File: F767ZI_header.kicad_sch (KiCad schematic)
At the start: 24 parts, among them J1 I2C2_MD, J2 CAN1, J3 CAN2, J4 UART, J5 PowerBoard, J6 EMERSW_CON, J7 I2C1_default, J9 RESET_SW, SW1 SW_Push, U1 MCP2562-E-P, U2 MCP2562-E-P

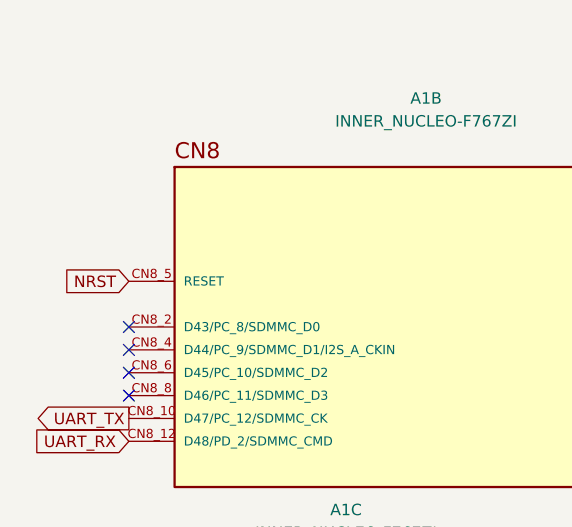
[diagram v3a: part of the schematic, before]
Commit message: SCH: Add CN8_1 to NUCLEO lib
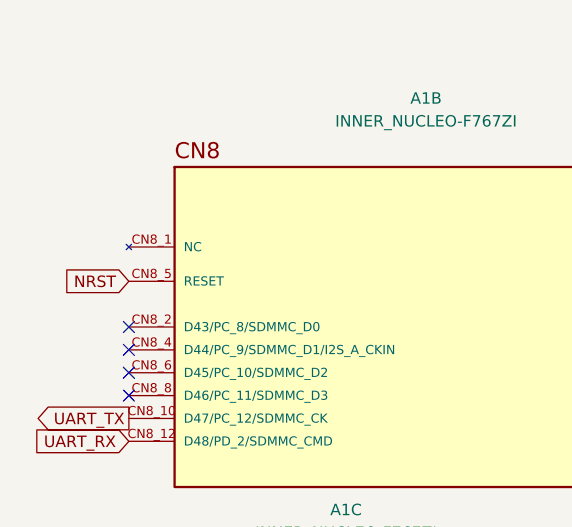
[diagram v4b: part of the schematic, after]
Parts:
- A1: footprint NUCLEO-F767ZI:INNER_ST_NUCLEO-F767ZI -> NUCLEO-F767ZI:ST_NUCLEO-F767ZI
- C1, C2, C3, C4: footprint (none) -> Capacitor_THT:C_Disc_D5.0mm_W2.5mm_P2.50mm
- J7: footprint (none) -> Connector_JST:JST_XA_B04B-XASK-1_1x04_P2.50mm_Vertical
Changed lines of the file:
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@@
 			)
 		)
-		(property "Footprint" ""
+		(property "Footprint" "Capacitor_THT:C_Disc_D5.0mm_W2.5mm_P2.50mm"
 			(at 156.21 91.44 0)
 			(effects
@@
 			)
 		)
-		(property "Footprint" ""
+		(property "Footprint" "Capacitor_THT:C_Disc_D5.0mm_W2.5mm_P2.50mm"
 			(at 156.21 130.81 0)
 			(effects
@@
 	)
 	(symbol
+		(lib_name "INNER_NUCLEO-F767ZI_1")
 		(lib_id "NUCLEO-F767ZI:INNER_NUCLEO-F767ZI")
 		(at 67.31 54.61 0)
@@
 			)
 		)
-		(property "Footprint" "NUCLEO-F767ZI:INNER_ST_NUCLEO-F767ZI"
+		(property "Footprint" "NUCLEO-F767ZI:ST_NUCLEO-F767ZI"
 			(at 67.31 54.61 0)
 			(effects
@@
 		(pin "CN10_12"
 		)
+		(pin "CN8_1-UA"
+		)
+		(pin "CN8_1-UC"
+		)
+		(pin "CN8_1"
+		)
+		(pin "CN8_1-UD"
+		)
 		(instances
 			(project "F767ZI_header"
@@
 			)
 		)
-		(property "Footprint" "NUCLEO-F767ZI:INNER_ST_NUCLEO-F767ZI"
+		(property "Footprint" "NUCLEO-F767ZI:ST_NUCLEO-F767ZI"
 			(at 232.41 50.8 0)
 			(effects
@@
 			)
 		)
-		(property "Footprint" ""
+		(property "Footprint" "Connector_JST:JST_XA_B04B-XASK-1_1x04_P2.50mm_Vertical"
 			(at 138.43 149.86 0)
 			(effects
@@
 			)
 		)
-		(property "Footprint" "NUCLEO-F767ZI:INNER_ST_NUCLEO-F767ZI"
+		(property "Footprint" "NUCLEO-F767ZI:ST_NUCLEO-F767ZI"
 			(at 57.15 109.22 0)
 			(effects
@@
 			)
 		)
-		(property "Footprint" ""
+		(property "Footprint" "Capacitor_THT:C_Disc_D5.0mm_W2.5mm_P2.50mm"
 			(at 147.32 91.44 0)
 			(effects
@@
 			)
 		)
-		(property "Footprint" "NUCLEO-F767ZI:INNER_ST_NUCLEO-F767ZI"
+		(property "Footprint" "NUCLEO-F767ZI:ST_NUCLEO-F767ZI"
 			(at 242.57 110.49 0)
 			(effects
@@
 			)
 		)
-		(property "Footprint" ""
+		(property "Footprint" "Capacitor_THT:C_Disc_D5.0mm_W2.5mm_P2.50mm"
 			(at 147.32 130.81 0)
 			(effects

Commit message: SCH&PCB: Fix NUCLEO ilb
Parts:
- A1: footprint NUCLEO-F767ZI:ST_NUCLEO-F767ZI -> NUCLEO-F767ZI:INNER_ST_NUCLEO-F767ZI
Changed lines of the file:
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@@
 			)
 		)
-		(property "Footprint" "NUCLEO-F767ZI:ST_NUCLEO-F767ZI"
+		(property "Footprint" "NUCLEO-F767ZI:INNER_ST_NUCLEO-F767ZI"
 			(at 67.31 54.61 0)
 			(effects
@@
 			)
 		)
-		(property "Footprint" "NUCLEO-F767ZI:ST_NUCLEO-F767ZI"
+		(property "Footprint" "NUCLEO-F767ZI:INNER_ST_NUCLEO-F767ZI"
 			(at 232.41 50.8 0)
 			(effects
@@
 			)
 		)
-		(property "Footprint" "NUCLEO-F767ZI:ST_NUCLEO-F767ZI"
+		(property "Footprint" "NUCLEO-F767ZI:INNER_ST_NUCLEO-F767ZI"
 			(at 57.15 109.22 0)
 			(effects
@@
 			)
 		)
-		(property "Footprint" "NUCLEO-F767ZI:ST_NUCLEO-F767ZI"
+		(property "Footprint" "NUCLEO-F767ZI:INNER_ST_NUCLEO-F767ZI"
 			(at 242.57 110.49 0)
 			(effects

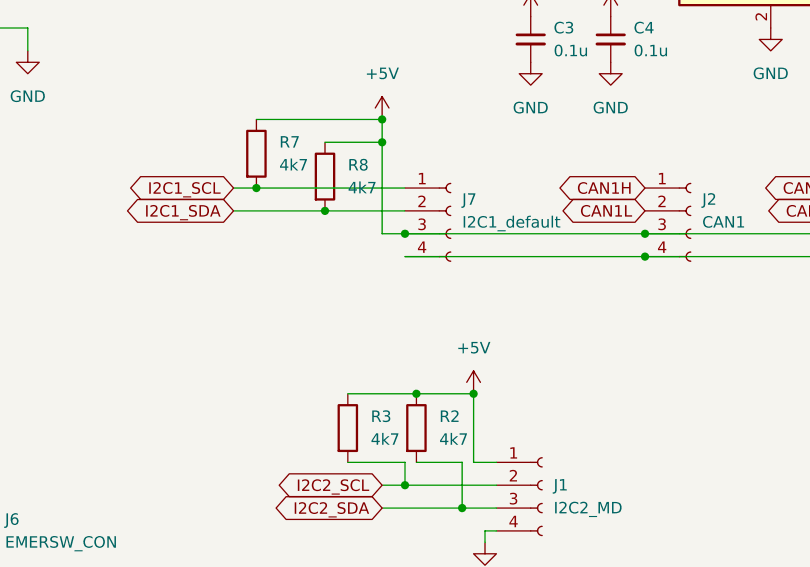
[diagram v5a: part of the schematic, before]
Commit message: SCH: Connected GND & all transmission PINs
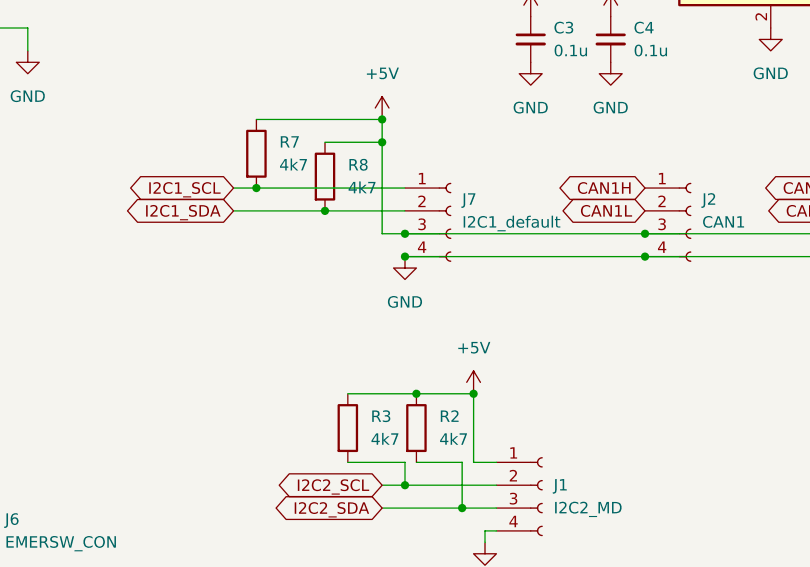
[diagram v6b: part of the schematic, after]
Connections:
- net GND: now also J2.4 (Pin_4), J3.4 (Pin_4), J4.4 (Pin_4), J7.4 (Pin_4)
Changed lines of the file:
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@@
 	)
 	(junction
+		(at 133.35 154.94)
+		(diameter 0)
+		(color 0 0 0 0)
+	)
+	(junction
 		(at 82.55 184.15)
 		(diameter 0)
@@
 					(unit 1)
 				)
+			)
+		)
+	)
+	(symbol
+		(lib_id "power:GND")
+		(at 133.35 154.94 0)
+		(unit 1)
+		(exclude_from_sim no)
+		(in_bom yes)
+		(on_board yes)
+		(dnp no)
+		(fields_autoplaced yes)
+		(property "Reference" "#PWR032"
+			(at 133.35 161.29 0)
+			(effects
+				(font
+					(size 1.27 1.27)
+				)
+				(hide yes)
+			)
+		)
+		(property "Value" "GND"
+			(at 133.35 160.02 0)
+			(effects
+				(font
+					(size 1.27 1.27)
+				)
+			)
+		)
+		(property "Footprint" ""
+			(at 133.35 154.94 0)
+			(effects
+				(font
+					(size 1.27 1.27)
+				)
+				(hide yes)
+			)
+		)
+		(property "Datasheet" ""
+			(at 133.35 154.94 0)
+			(effects
+				(font
+					(size 1.27 1.27)
+				)
+				(hide yes)
+			)
+		)
+		(property "Description" "Power symbol creates a global label with name \"GND\" , ground"
+			(at 133.35 154.94 0)
+			(effects
+				(font
+					(size 1.27 1.27)
+				)
+				(hide yes)
+			)
+		)
+		(pin "1"
+		)
+		(instances
+			(project "F767ZI_header"
+				(path "/b49c86d0-897f-4af2-adc1-6b5936ca98fe"
+					(reference "#PWR032")
+					(unit 1)
+				)

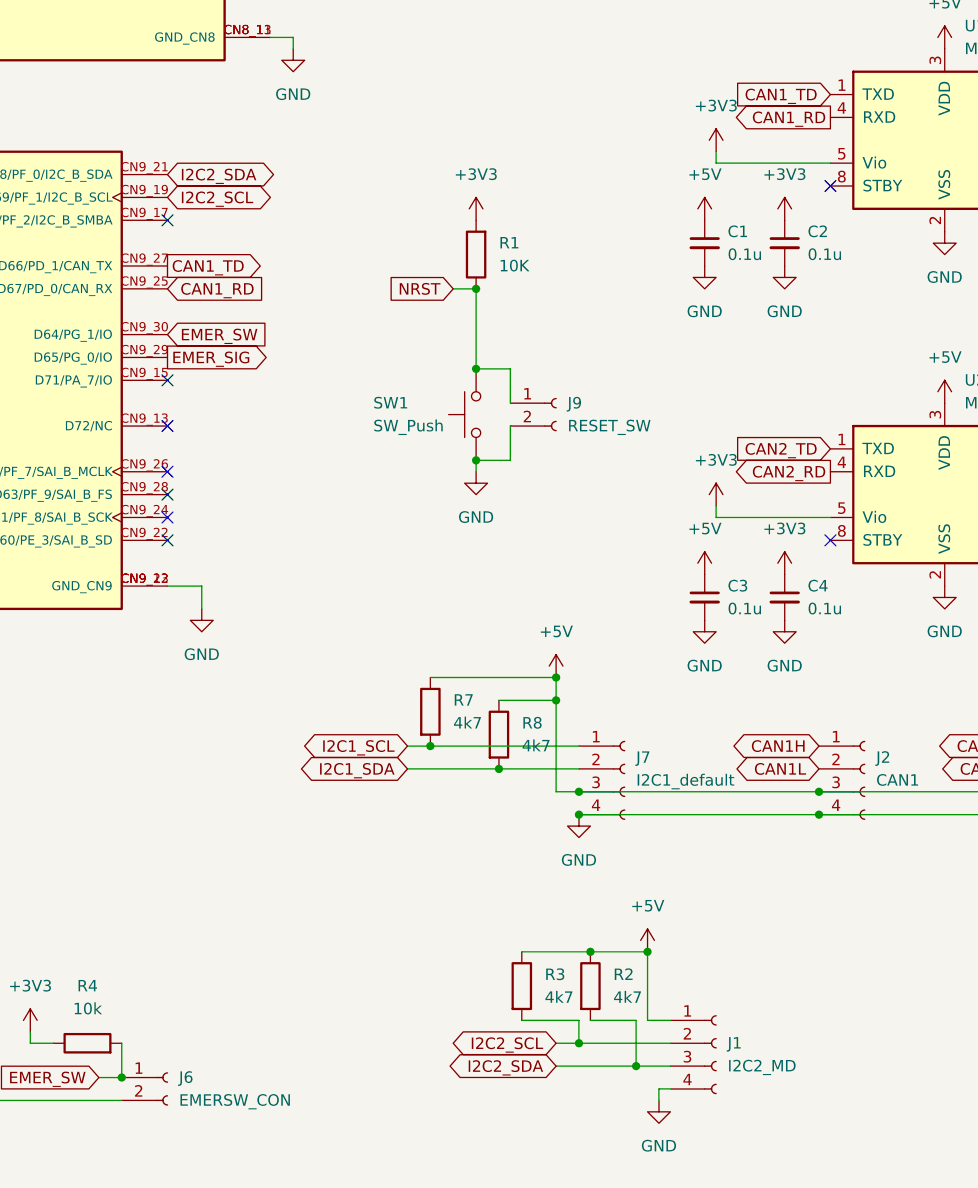
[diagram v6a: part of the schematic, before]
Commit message: SCH: I2C(MD)を削除
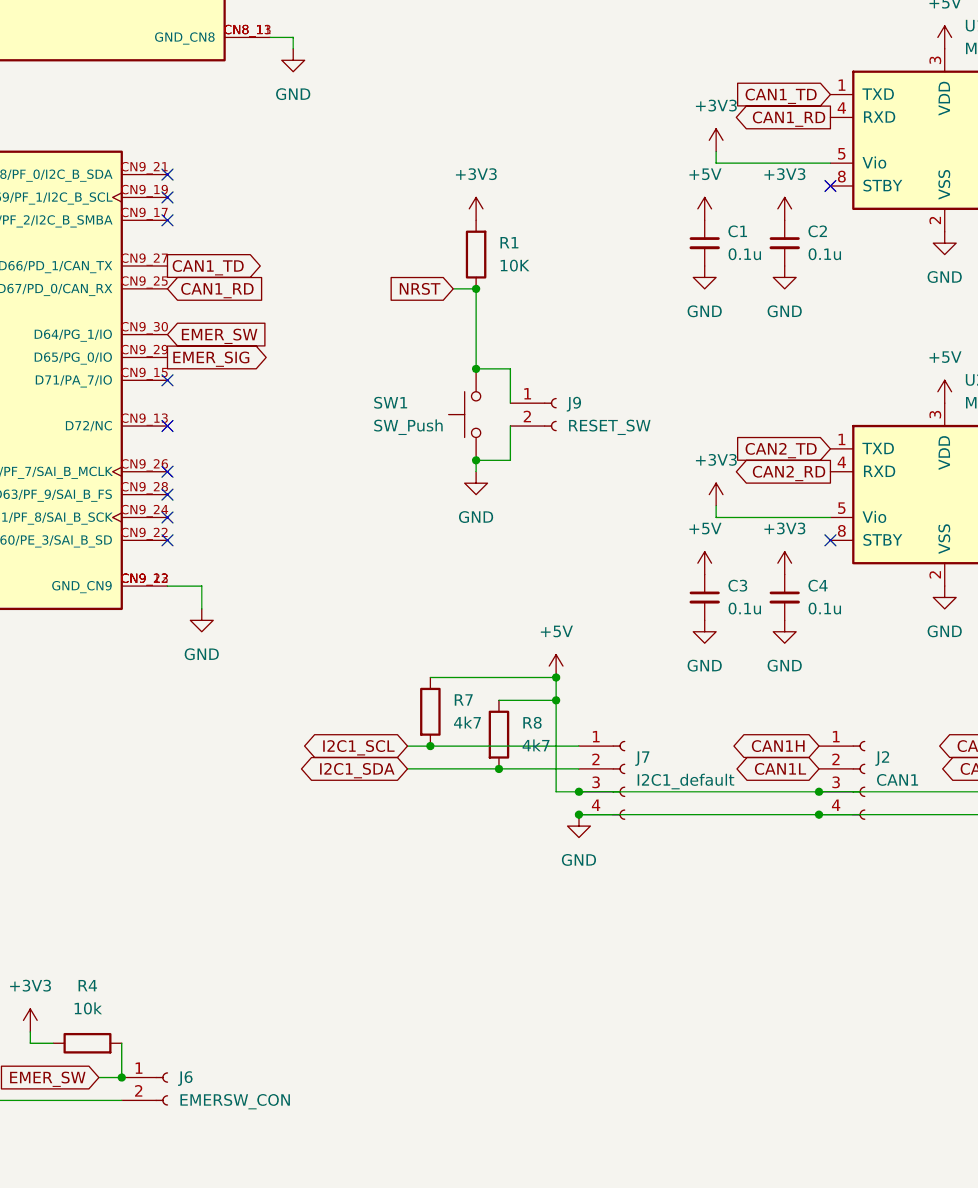
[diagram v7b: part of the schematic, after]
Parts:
- removed J1: I2C2_MD, Connector_JST:JST_XA_B04B-XASK-1_1x04_P2.50mm_Vertical, symbol Connector:Conn_01x04_Socket
- removed R2, R3: 4k7, Resistor_THT:R_Axial_DIN0207_L6.3mm_D2.5mm_P7.62mm_Horizontal, symbol Device:R
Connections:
- net I2C2_SCL: no longer names the net of A1.CN9_19 (D69/PF_1/I2C_B_SCL)
- net I2C2_SDA: no longer names the net of A1.CN9_21 (D68/PF_0/I2C_B_SDA)
- no-connect marks 77 -> 79

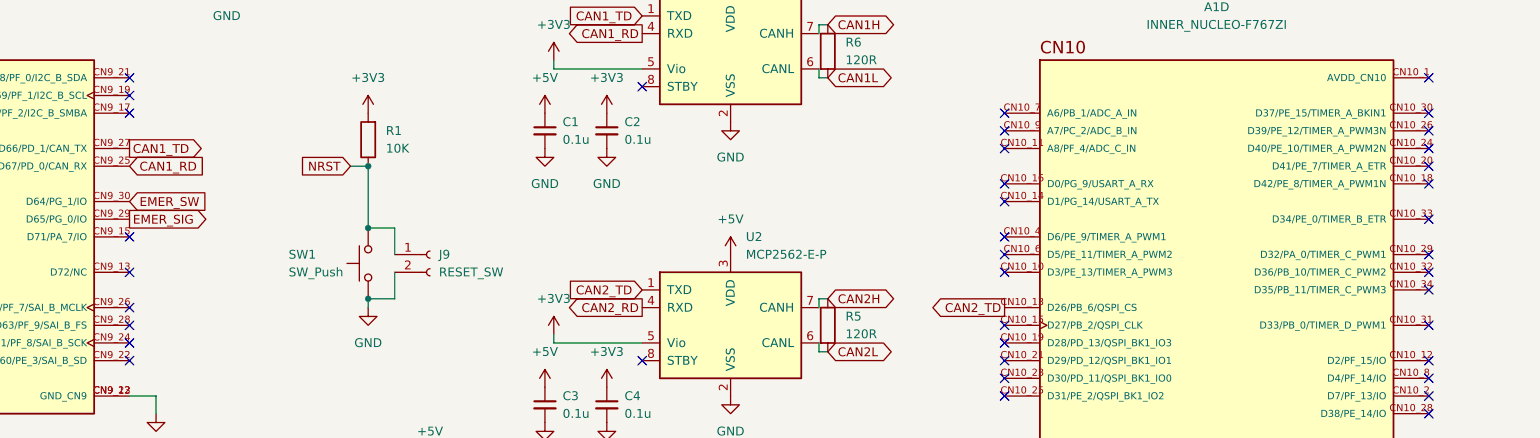
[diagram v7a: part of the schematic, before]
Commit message: PCB/SCH: EMER_SIGのピン変更、コネクタ再配置
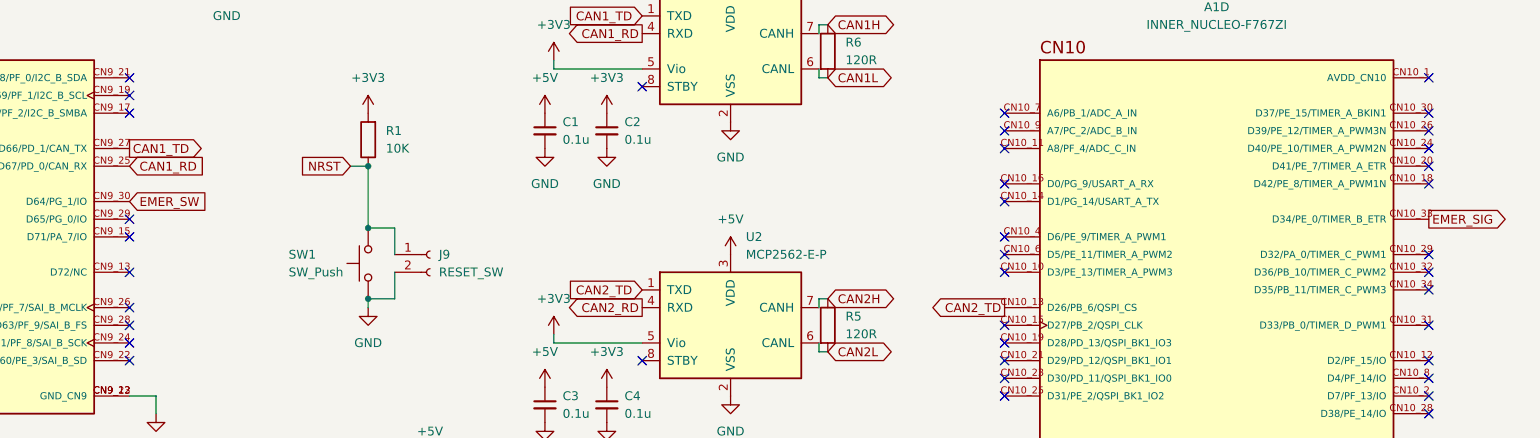
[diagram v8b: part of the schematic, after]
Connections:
- net EMER_SIG: now also A1.CN10_33 (D34/PE_0/TIMER_B_ETR); no longer A1.CN9_29 (D65/PG_0/IO)
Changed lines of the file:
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@@
+	)
+	(no_connect
+		(at 87.63 104.14)
 	)
 	(no_connect
@@
 	(no_connect
 		(at 87.63 86.36)
-	)
-	(no_connect
-		(at 274.32 104.14)
 	)
 	(no_connect
@@
 	(global_label "EMER_SIG"
 		(shape output)
-		(at 87.63 104.14 0)
+		(at 274.32 104.14 0)
 		(fields_autoplaced yes)
 		(effects
@@
 		)
 		(property "Intersheetrefs" "${INTERSHEET_REFS}"
-			(at 99.6865 104.14 0)
-			(effects
-				(font
+			(at 286.3765 104.14 0)
+			(effects
+				(font
